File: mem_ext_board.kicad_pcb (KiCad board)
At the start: 2 copper layers, 34.9 x 38.1 mm, 13 parts, among them J1 Conn_02x05_Odd_Even, J2 Conn_02x02_Odd_Even, J3 Conn_02x16_Row_Letter_First, U1 74LS30, U2 AS6C1008-xxT, U4 74LS86

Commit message: Updated board to hopefully final shape
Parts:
- added J4: Conn_02x05_Odd_Even, Connector_PinSocket_2.54mm:PinSocket_2x05_P2.54mm_Vertical, B.Cu at (167.4, 50.2)
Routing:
- net /A21: track 5.21 -> 54.0 mm
- net /A20: track 8.18 -> 53.8 mm, vias 0 -> 1
- net /A19: track 22.9 -> 67.4 mm
- net /A17: track 40.2 -> 84.3 mm, vias 3 -> 4
- net /A18: track 45.3 -> 87.5 mm
- net /A16: track 32.0 -> 68.3 mm, vias 0 -> 1
- net GND: track 15.5 -> 36.5 mm
- net +5V: track 62.7 -> 70.3 mm
- net /~{WR}: track 14.4 -> 15.3 mm
- net /~{RD}: track 41.5 -> 42.1 mm, vias 2 -> 3
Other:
- board size 34.9 x 38.1 mm -> 40.6 x 66.7 mm

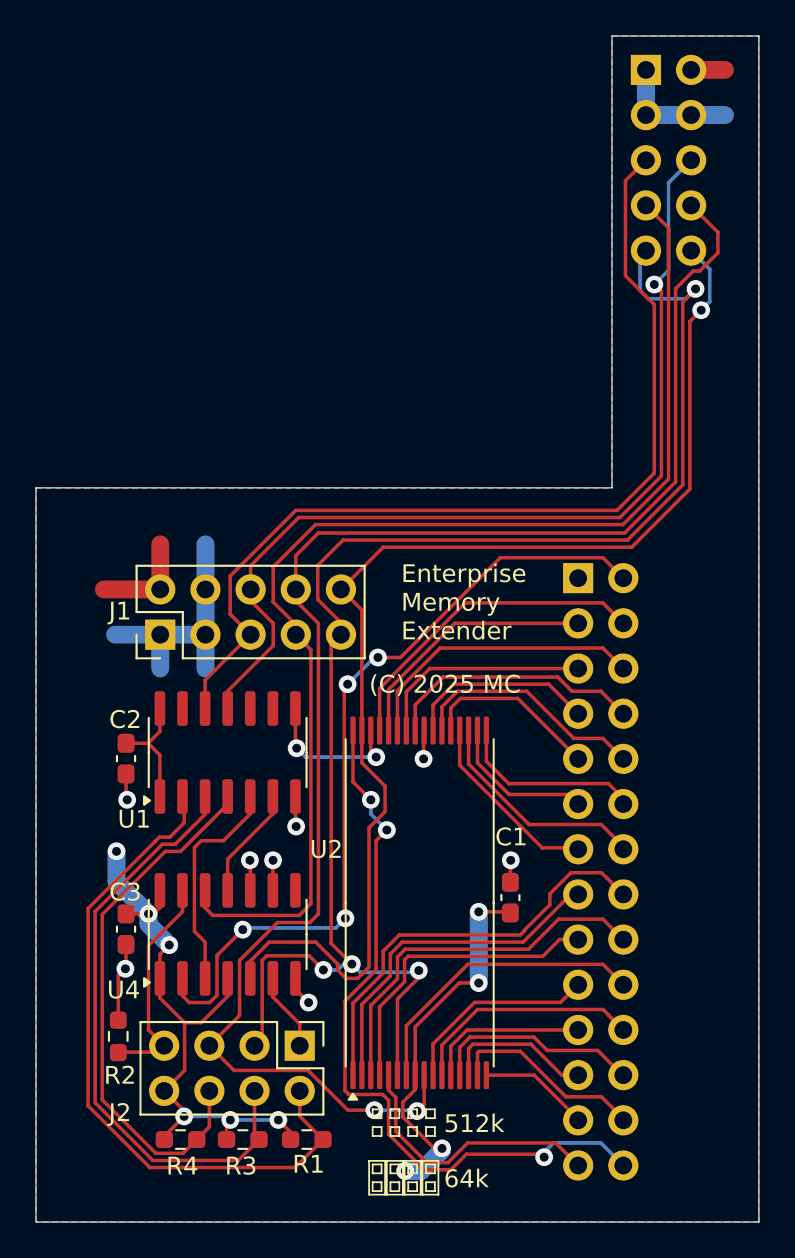
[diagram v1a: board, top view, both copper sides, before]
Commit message: Moved connector to match mainboard layout.
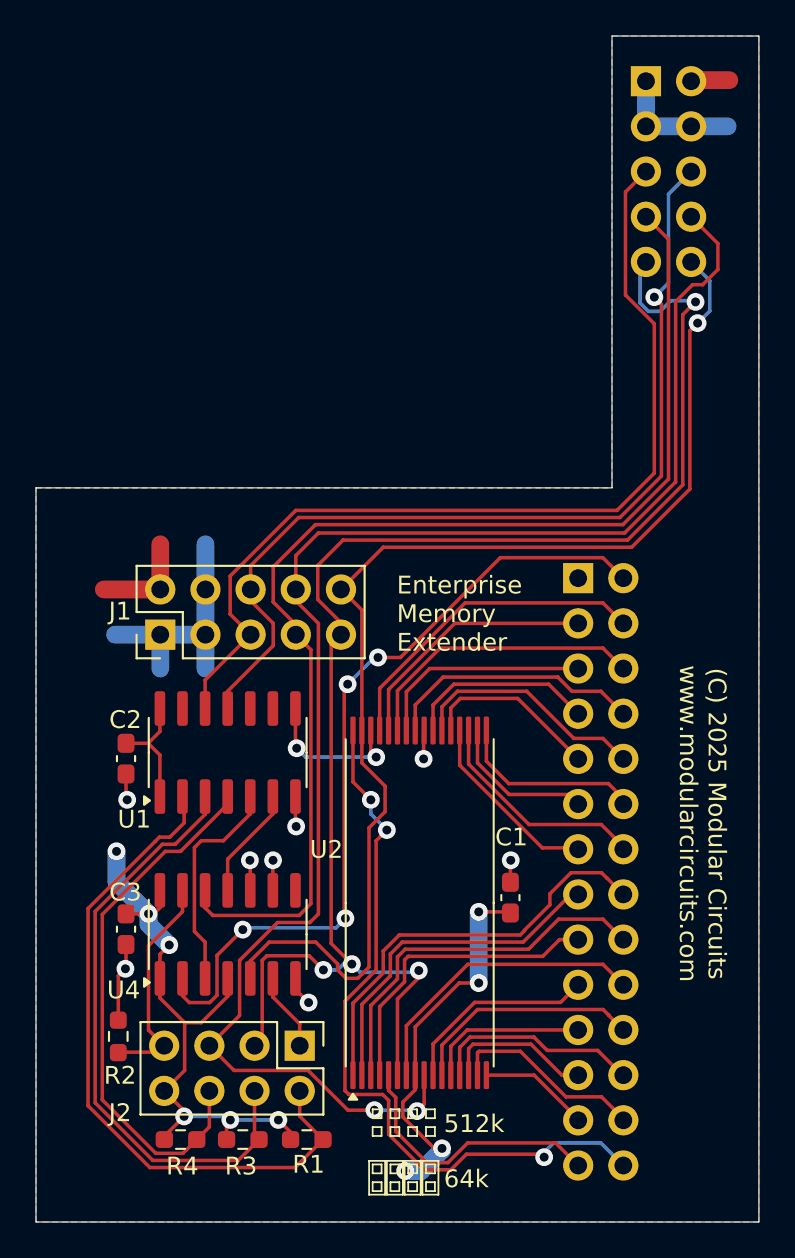
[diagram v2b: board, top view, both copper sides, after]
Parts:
- moved J4 0.63 mm to (167.4, 50.8)
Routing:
- net /A20: track 53.8 -> 52.9 mm
- net /A21: track 54.0 -> 53.3 mm
- net /A19: track 67.4 -> 66.7 mm
- net /A16: track 68.3 -> 67.7 mm
- net /A17: track 84.3 -> 83.6 mm
- net /A18: track 87.5 -> 87.0 mm
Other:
- board text added: "(C) 2025 Modular Circuits www.modularcircuits.com"
- board text removed: "(C) 2025 MC"

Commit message: Added support for 1Mbit part, release package added.
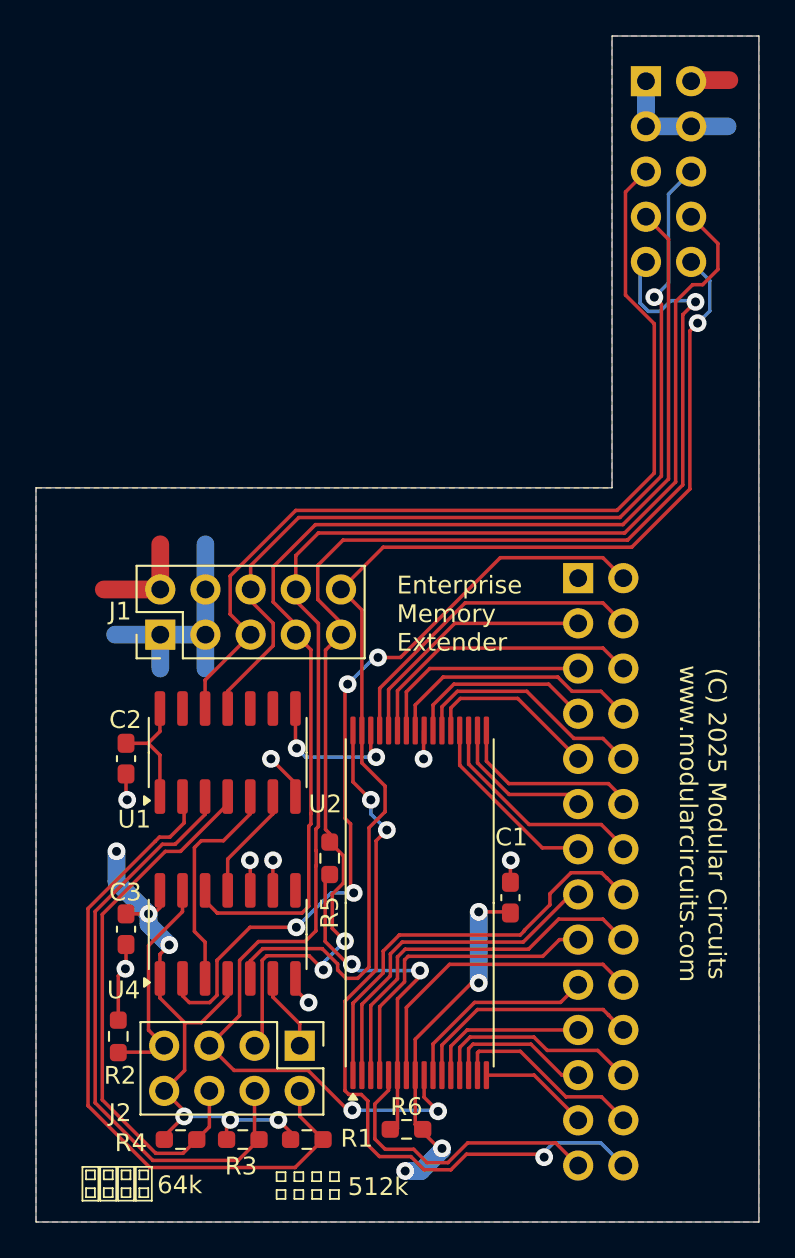
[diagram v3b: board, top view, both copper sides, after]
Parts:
- added R5: 0, Resistor_SMD:R_0603_1608Metric_Pad0.98x0.95mm_HandSolder, F.Cu at (149.6, 94.5)
- added R6: 10k, Resistor_SMD:R_0603_1608Metric_Pad0.98x0.95mm_HandSolder, F.Cu at (154.0, 109.7)
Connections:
- U2 pad 6: /A17 -> Net-(U2-CS2/A17)
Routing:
- net Net-(U2-CS2/A17): track 0.00 -> 19.7 mm, vias 0 -> 2
- net /A17: track 83.6 -> 73.0 mm, vias 4 -> 3
- net /A18: track 87.0 -> 88.8 mm
- net /~{WR}: track 15.3 -> 16.9 mm
- net +5V: track 70.6 -> 69.5 mm
- net GND: track 36.6 -> 37.6 mm
- net /A15: track 16.9 -> 17.5 mm

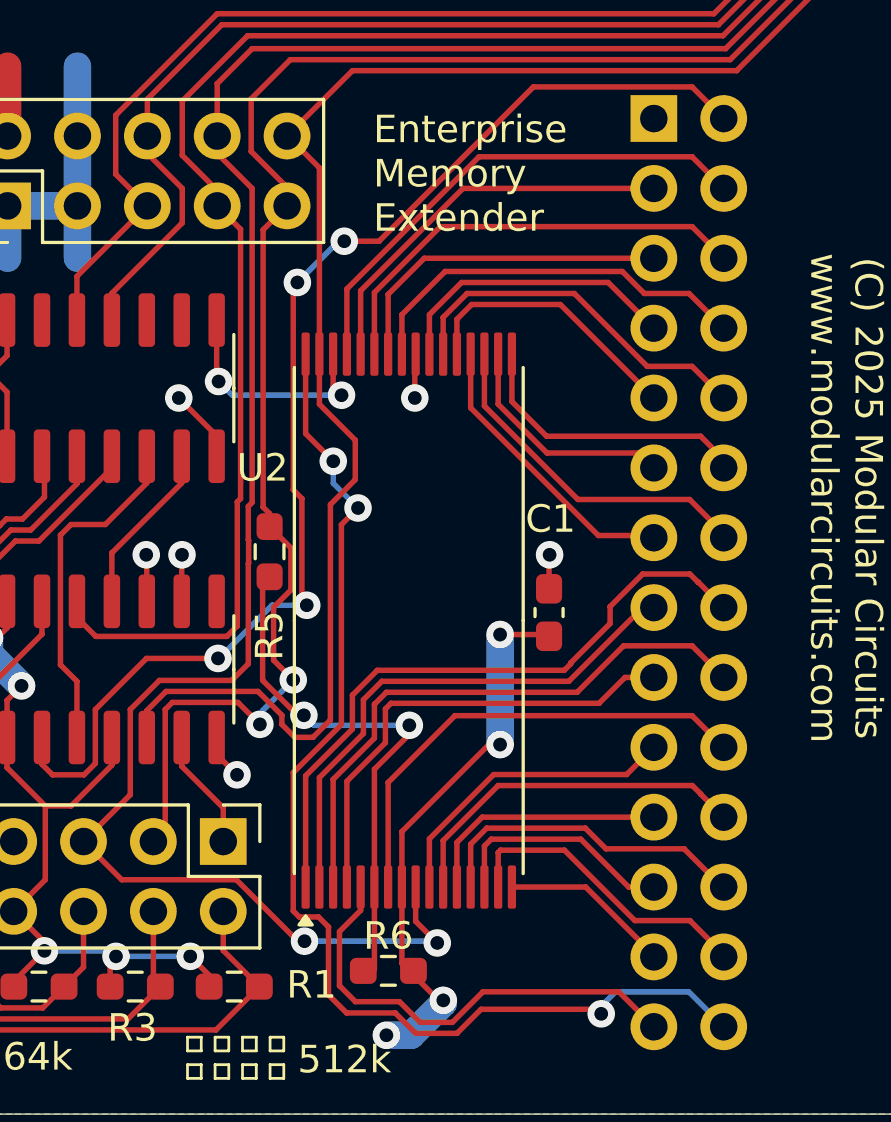
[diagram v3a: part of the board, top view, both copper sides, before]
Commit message: Universal memory footprint added: multiple package sizes are supported.
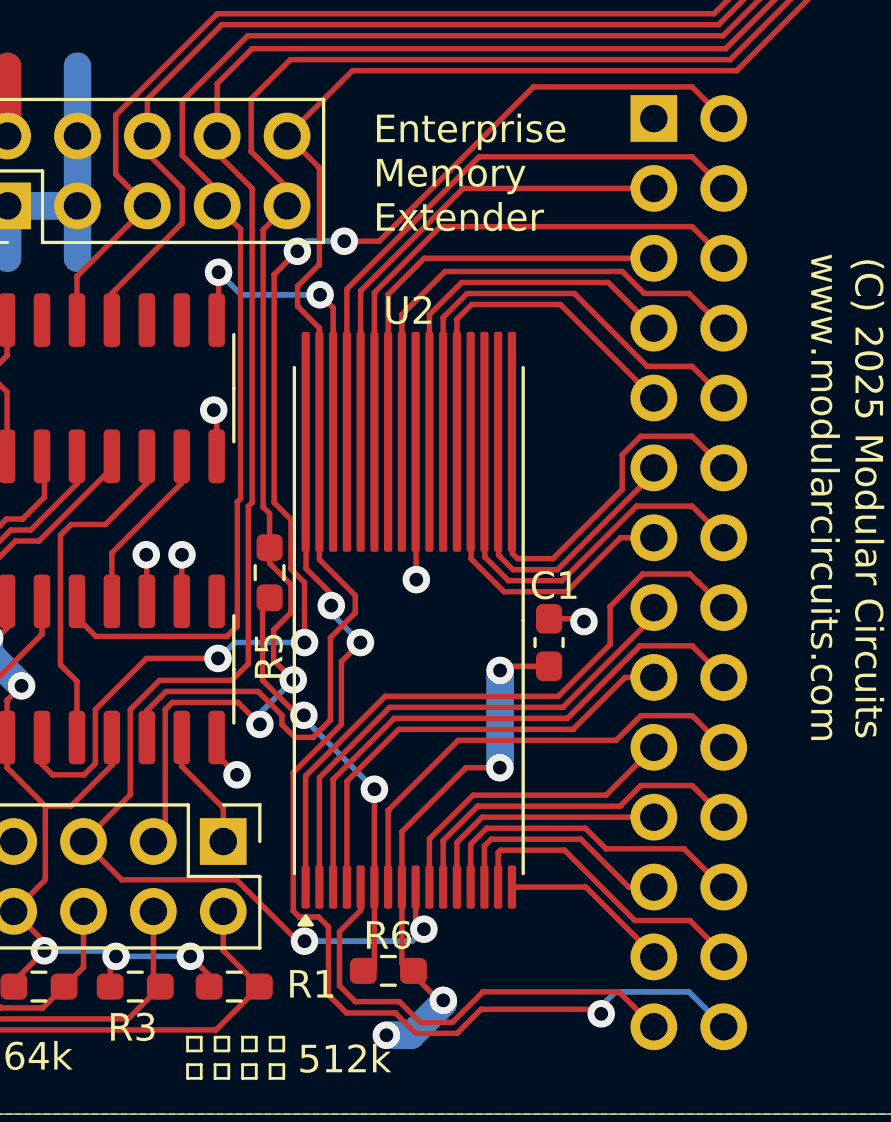
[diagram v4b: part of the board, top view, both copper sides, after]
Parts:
- U2: footprint Package_SO:TSOP-I-32_18.4x8mm_P0.5mm -> mem_ext_board:TSOP-I-32_11-18.4x8mm_P0.5mm
- moved C1 1.09 mm to (159.8, 97.8)
- moved R5 0.76 mm to (149.6, 95.2)
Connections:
- net Net-(U2-CS2/A17) renamed /MA14
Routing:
- net /A7: track 10.6 -> 18.1 mm
- net /D7: track 18.5 -> 25.0 mm
- net /D6: track 14.5 -> 21.0 mm
- net /D4: track 12.4 -> 18.9 mm
- net /D3: track 14.6 -> 21.1 mm
- net /D1: track 13.5 -> 20.0 mm
- net /D2: track 10.8 -> 17.3 mm
- net /D0: track 10.1 -> 16.6 mm
- net /D5: track 16.4 -> 22.9 mm
- net /A6: track 8.44 -> 14.8 mm
- net /~{CS}: track 8.56 -> 14.7 mm
- net GND: track 37.6 -> 43.3 mm
- net /A5: track 12.7 -> 18.0 mm
- net /A4: track 10.6 -> 15.4 mm
- net /MA14: track 19.7 -> 15.9 mm
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
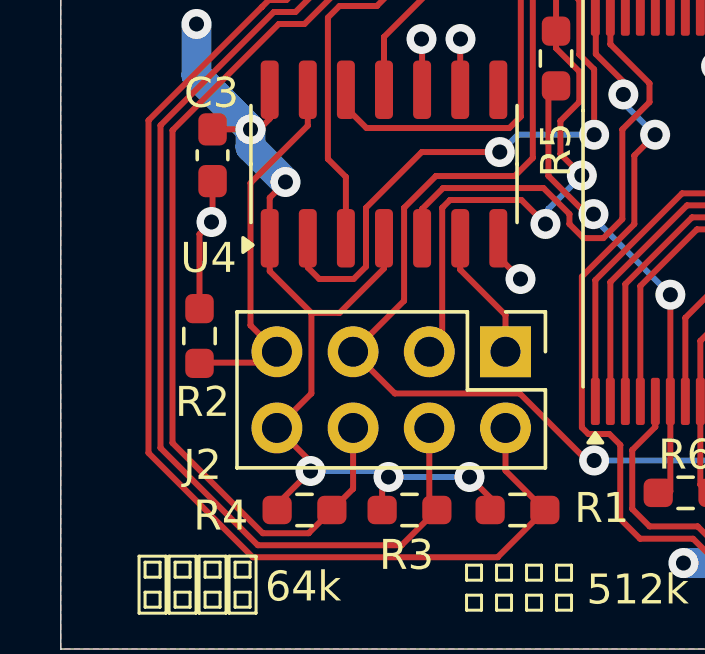
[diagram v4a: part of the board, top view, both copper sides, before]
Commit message: Flipped jumper setting so that operation matches silk-screen.
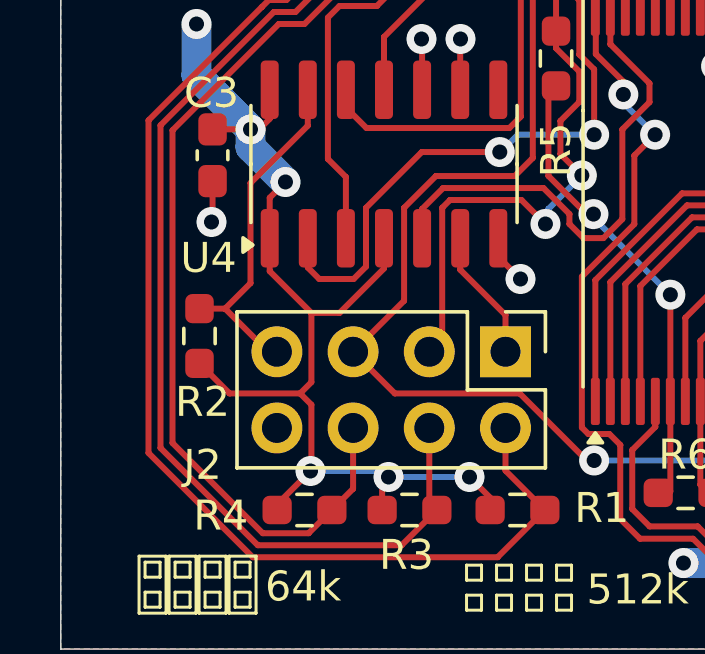
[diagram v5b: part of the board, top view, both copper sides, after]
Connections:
- J2 pad 8: +5V -> GND
- R2 pad 1: Net-(J2-Pin_7) -> +5V
- R2 pad 2: GND -> Net-(J2-Pin_7)
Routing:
- net +5V: track 68.7 -> 72.1 mm
- net GND: track 43.3 -> 40.3 mm
- net Net-(J2-Pin_7): track 12.6 -> 11.6 mm
